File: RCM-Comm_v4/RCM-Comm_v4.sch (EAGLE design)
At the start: 27 parts, among them J1 BLACKFIN_HEADER, J2 2199230-4

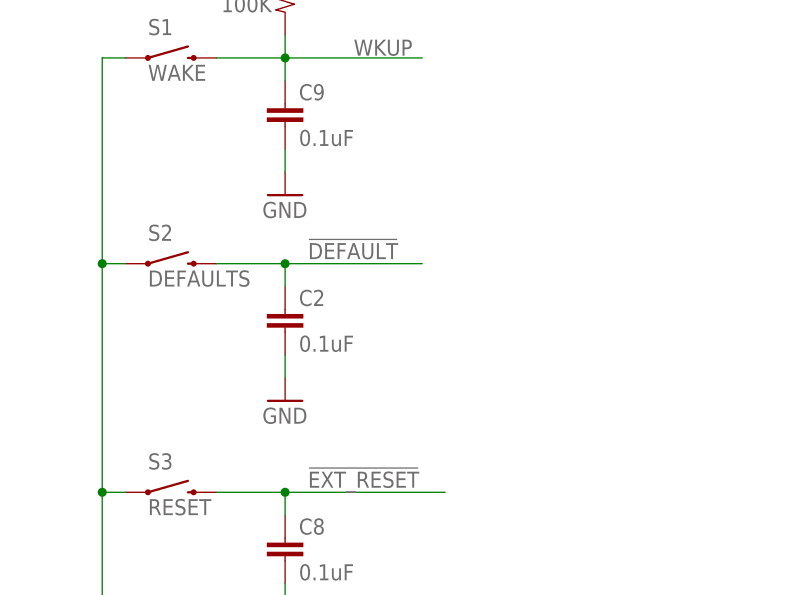
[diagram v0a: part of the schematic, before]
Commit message: Added DEFAULT ENABLE header back in, re-rendered top and bottom for approval.
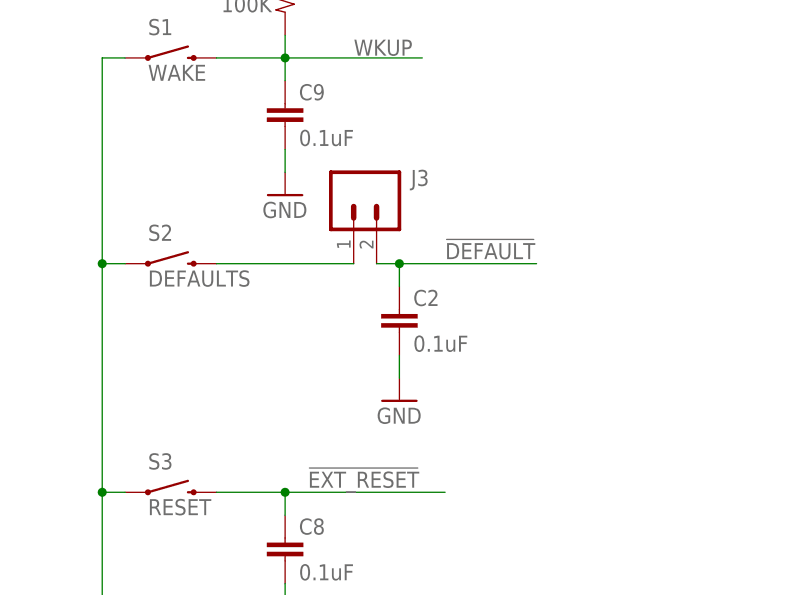
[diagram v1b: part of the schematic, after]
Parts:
- added J3: (no value), SparkFun-Connectors:CONN_02
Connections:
- new net N$1: J3.1, S2.2
- net !DEFAULT!: now also J3.2; no longer S2.2
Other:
- note added: "12/24/2018 v4.0 first release - Swapped radios to xPico 240 with new M.2 connector - removed extra circutry that 240 doesn't support"
- note added: "Connect to allow default button to work"
- note added: "xPico 240 with M.2 connector"
- note removed: "05/30/16 BPS Removed big holes with copper ring, added same dia but normal holes, moved them so they sit better on other boards in the stack."
- moved on the sheet: C2
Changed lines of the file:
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@@
 <layer number="230" name="230bmp" color="7" fill="1" visible="no" active="yes"/>
 <layer number="231" name="231bmp" color="7" fill="1" visible="no" active="yes"/>
+<layer number="232" name="Eagle3D_PG2" color="7" fill="1" visible="yes" active="yes"/>
+<layer number="233" name="Eagle3D_PG3" color="7" fill="1" visible="yes" active="yes"/>
 <layer number="248" name="Housing" color="7" fill="1" visible="yes" active="yes"/>
 <layer number="249" name="Edge" color="7" fill="1" visible="yes" active="yes"/>
@@
 <part name="R10" library="spark_fun" deviceset="RESISTOR" device="0603-RES" value="100K"/>
 <part name="P+10" library="spark_fun" deviceset="VCC" device=""/>
+<part name="J3" library="SparkFun-Connectors" library_urn="urn:adsk.eagle:library:513" deviceset="CONN_02" device="" package3d_urn="urn:adsk.eagle:package:38039/1"/>
 </parts>
 <sheets>
@@
 governing permissions and limitations under the License.</text>
 <text x="5.08" y="177.8" size="5.08" layer="94">RCM-Comm Board v4.0</text>
-<text x="139.7" y="180.34" size="1.27" layer="98">05/30/16 BPS Removed big holes with copper ring, added same dia but normal holes,
-moved them so they sit better on other boards in the stack.</text>
+<text x="114.3" y="167.64" size="1.27" layer="98">12/24/2018 v4.0 first release
+  - Swapped radios to xPico 240 with new M.2 connector
+  - removed extra circutry that 240 doesn't support</text>
+<text x="113.03" y="77.47" size="1.778" layer="98">Connect to allow default button to work</text>
+<text x="193.04" y="58.42" size="1.778" layer="98">xPico 240 with M.2 connector</text>
 </plain>
 <instances>
@@
 <attribute name="VALUE" x="76.2" y="27.94" size="1.778" layer="96"/>
 </instance>
-<instance part="C2" gate="G$1" x="99.06" y="63.5" smashed="yes">
-<attribute name="NAME" x="100.584" y="66.421" size="1.778" layer="95"/>
-<attribute name="VALUE" x="100.584" y="61.341" size="1.778" layer="96"/>
+<instance part="C2" gate="G$1" x="111.76" y="63.5" smashed="yes">
+<attribute name="NAME" x="113.284" y="66.421" size="1.778" layer="95"/>
+<attribute name="VALUE" x="113.284" y="61.341" size="1.778" layer="96"/>
 </instance>
 <instance part="C8" gate="G$1" x="99.06" y="38.1" smashed="yes">
@@
 <attribute name="VALUE" x="100.584" y="84.201" size="1.778" layer="96"/>
 </instance>
-<instance part="GND10" gate="1" x="99.06" y="55.88" smashed="yes">
-<attribute name="VALUE" x="96.52" y="53.34" size="1.778" layer="96"/>
+<instance part="GND10" gate="1" x="111.76" y="55.88" smashed="yes">
+<attribute name="VALUE" x="109.22" y="53.34" size="1.778" layer="96"/>
 </instance>
 <instance part="GND11" gate="1" x="99.06" y="30.48" smashed="yes">
@@
 <instance part="P+10" gate="1" x="7.62" y="35.56" smashed="yes">
 <attribute name="VALUE" x="7.874" y="35.56" size="1.778" layer="96" rot="R270"/>
+</instance>
+<instance part="J3" gate="G$1" x="106.68" y="78.74" smashed="yes" rot="R270">
+<attribute name="VALUE" x="101.854" y="81.28" size="1.778" layer="96" font="vector" rot="R270"/>
+<attribute name="NAME" x="113.03" y="79.756" size="1.778" layer="95" font="vector"/>
 </instance>
 </instances>
@@
 <pinref part="C2" gate="G$1" pin="2"/>
 <pinref part="GND10" gate="1" pin="GND"/>
-<wire x1="99.06" y1="60.96" x2="99.06" y2="58.42" width="0.1524" layer="91"/>
+<wire x1="111.76" y1="60.96" x2="111.76" y2="58.42" width="0.1524" layer="91"/>
 </segment>
 <segment>
@@
 <net name="!DEFAULT!" class="0">
 <segment>
-<pinref part="S2" gate="G$1" pin="2"/>
-<wire x1="91.44" y1="71.12" x2="99.06" y2="71.12" width="0.1524" layer="91"/>
-<label x="101.6" y="71.628" size="1.778" layer="95"/>
+<label x="116.84" y="71.628" size="1.778" layer="95"/>
 <pinref part="C2" gate="G$1" pin="1"/>
-<wire x1="99.06" y1="71.12" x2="114.3" y2="71.12" width="0.1524" layer="91"/>
-<wire x1="99.06" y1="68.58" x2="99.06" y2="71.12" width="0.1524" layer="91"/>
-<junction x="99.06" y="71.12"/>
+<wire x1="111.76" y1="71.12" x2="127" y2="71.12" width="0.1524" layer="91"/>
+<wire x1="111.76" y1="68.58" x2="111.76" y2="71.12" width="0.1524" layer="91"/>
+<pinref part="J3" gate="G$1" pin="2"/>
+<wire x1="109.22" y1="71.12" x2="111.76" y2="71.12" width="0.1524" layer="91"/>
+<junction x="111.76" y="71.12"/>
 </segment>
 <segment>
@@
 <wire x1="20.32" y1="30.48" x2="30.48" y2="30.48" width="0.1524" layer="91"/>
 <label x="22.86" y="30.48" size="1.778" layer="95"/>
+</segment>
+</net>
+<net name="N$1" class="0">
+<segment>
+<pinref part="S2" gate="G$1" pin="2"/>
+<pinref part="J3" gate="G$1" pin="1"/>
+<wire x1="91.44" y1="71.12" x2="106.68" y2="71.12" width="0.1524" layer="91"/>
 </segment>
 </net>
@@
 which will not be processed correctly with this version.
 </note>
+<note version="8.2" severity="warning">
+Since Version 8.2, EAGLE supports online libraries. The ids
+of those online libraries will not be understood (or retained)
+with this version.
+</note>
+<note version="8.3" severity="warning">
+Since Version 8.3, EAGLE supports URNs for individual library
+assets (packages, symbols, and devices). The URNs of those assets
+will not be understood (or retained) with this version.
+</note>
+<note version="8.3" severity="warning">
+Since Version 8.3, EAGLE supports the association of 3D packages
+with devices in libraries, schematics, and board files. Those 3D
+packages will not be understood (or retained) with this version.
+</note>
 </compatibility>

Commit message: Added WLAN Led on configurable pin (CP) #1.
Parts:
- added LED3: GREEN, spark_fun:LED0603
- added R1: 330, spark_fun:RESISTOR0603-RES
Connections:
- removed net N$68: J2.50
- new net N$2: LED3.A, R1.2
- new net WLAN0: J2.50, R1.1
- net GND: now also LED3.C
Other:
- moved on the sheet: LED1, LED2, R3, R5
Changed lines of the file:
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@@
 <part name="P+10" library="spark_fun" deviceset="VCC" device=""/>
 <part name="J3" library="SparkFun-Connectors" library_urn="urn:adsk.eagle:library:513" deviceset="CONN_02" device="" package3d_urn="urn:adsk.eagle:package:38039/1"/>
+<part name="R1" library="spark_fun" deviceset="RESISTOR" device="0603-RES" value="330"/>
+<part name="LED3" library="spark_fun" deviceset="LED" device="0603" value="GREEN"/>
+<part name="GND1" library="supply1" deviceset="GND" device=""/>
 </parts>
 <sheets>
@@
 <attribute name="NAME" x="52.07" y="150.622" size="1.778" layer="95"/>
 </instance>
-<instance part="LED1" gate="G$1" x="15.24" y="76.2" smashed="yes">
-<attribute name="NAME" x="4.826" y="75.184" size="1.778" layer="95"/>
-<attribute name="VALUE" x="3.048" y="72.009" size="1.778" layer="96"/>
-</instance>
-<instance part="LED2" gate="G$1" x="55.88" y="60.96" smashed="yes">
-<attribute name="NAME" x="45.72" y="60.706" size="1.778" layer="95"/>
-<attribute name="VALUE" x="43.688" y="56.769" size="1.778" layer="96"/>
+<instance part="LED1" gate="G$1" x="15.24" y="73.66" smashed="yes">
+<attribute name="NAME" x="4.826" y="72.644" size="1.778" layer="95"/>
+<attribute name="VALUE" x="3.048" y="69.469" size="1.778" layer="96"/>
+</instance>
+<instance part="LED2" gate="G$1" x="66.04" y="60.96" smashed="yes">
+<attribute name="NAME" x="55.88" y="60.706" size="1.778" layer="95"/>
+<attribute name="VALUE" x="53.848" y="56.769" size="1.778" layer="96"/>
 </instance>
 <instance part="GND2" gate="1" x="45.72" y="101.6" smashed="yes">
@@
 <attribute name="VALUE" x="40.64" y="2.54" size="1.778" layer="96"/>
 </instance>
-<instance part="R3" gate="G$1" x="15.24" y="63.5" smashed="yes" rot="R90">
-<attribute name="NAME" x="9.652" y="64.2366" size="1.778" layer="95"/>
-<attribute name="VALUE" x="8.382" y="60.96" size="1.778" layer="96"/>
-</instance>
-<instance part="R5" gate="G$1" x="55.88" y="71.12" smashed="yes" rot="R270">
-<attribute name="NAME" x="50.038" y="71.6026" size="1.778" layer="95"/>
-<attribute name="VALUE" x="48.768" y="68.58" size="1.778" layer="96"/>
+<instance part="R3" gate="G$1" x="15.24" y="60.96" smashed="yes" rot="R90">
+<attribute name="NAME" x="9.652" y="61.6966" size="1.778" layer="95"/>
+<attribute name="VALUE" x="8.382" y="58.42" size="1.778" layer="96"/>
+</instance>
+<instance part="R5" gate="G$1" x="66.04" y="71.12" smashed="yes" rot="R270">
+<attribute name="NAME" x="60.198" y="71.6026" size="1.778" layer="95"/>
+<attribute name="VALUE" x="58.928" y="68.58" size="1.778" layer="96"/>
 </instance>
 <instance part="FRAME1" gate="G$1" x="0" y="0" smashed="yes"/>
@@
 <attribute name="VALUE" x="87.884" y="13.081" size="1.778" layer="96"/>
 </instance>
-<instance part="GND6" gate="1" x="55.88" y="50.8" smashed="yes">
-<attribute name="VALUE" x="53.34" y="48.26" size="1.778" layer="96"/>
+<instance part="GND6" gate="1" x="66.04" y="50.8" smashed="yes">
+<attribute name="VALUE" x="63.5" y="48.26" size="1.778" layer="96"/>
 </instance>
 <instance part="S1" gate="G$1" x="86.36" y="93.98" smashed="yes">
@@
 <attribute name="VALUE" x="101.854" y="81.28" size="1.778" layer="96" font="vector" rot="R270"/>
 <attribute name="NAME" x="113.03" y="79.756" size="1.778" layer="95" font="vector"/>
+</instance>
+<instance part="R1" gate="G$1" x="40.64" y="71.12" smashed="yes" rot="R270">
+<attribute name="NAME" x="34.798" y="71.6026" size="1.778" layer="95"/>
+<attribute name="VALUE" x="33.528" y="68.58" size="1.778" layer="96"/>
+</instance>
+<instance part="LED3" gate="G$1" x="40.64" y="60.96" smashed="yes">
+<attribute name="NAME" x="30.48" y="60.706" size="1.778" layer="95"/>
+<attribute name="VALUE" x="28.448" y="56.769" size="1.778" layer="96"/>
+</instance>
+<instance part="GND1" gate="1" x="40.64" y="50.8" smashed="yes">
+<attribute name="VALUE" x="38.1" y="48.26" size="1.778" layer="96"/>
 </instance>
 </instances>
@@
 </segment>
 <segment>
-<wire x1="15.24" y1="58.42" x2="15.24" y2="53.34" width="0.1524" layer="91"/>
+<wire x1="15.24" y1="55.88" x2="15.24" y2="53.34" width="0.1524" layer="91"/>
 <pinref part="GND4" gate="1" pin="GND"/>
 <pinref part="R3" gate="G$1" pin="1"/>
@@
 <pinref part="LED2" gate="G$1" pin="C"/>
 <pinref part="GND6" gate="1" pin="GND"/>
-<wire x1="55.88" y1="55.88" x2="55.88" y2="53.34" width="0.1524" layer="91"/>
+<wire x1="66.04" y1="55.88" x2="66.04" y2="53.34" width="0.1524" layer="91"/>
 </segment>
 <segment>
@@
 <junction x="233.68" y="66.04"/>
 </segment>
+<segment>
+<pinref part="LED3" gate="G$1" pin="C"/>
+<pinref part="GND1" gate="1" pin="GND"/>
+<wire x1="40.64" y1="55.88" x2="40.64" y2="53.34" width="0.1524" layer="91"/>
+</segment>
 </net>
 <net name="VCC" class="0">
@@
 </segment>
 <segment>
-<wire x1="15.24" y1="83.82" x2="15.24" y2="78.74" width="0.1524" layer="91"/>
+<wire x1="15.24" y1="83.82" x2="15.24" y2="76.2" width="0.1524" layer="91"/>
 <pinref part="P+4" gate="1" pin="VCC"/>
 <pinref part="LED1" gate="G$1" pin="A"/>
@@
 <net name="N$3" class="0">
 <segment>
-<wire x1="15.24" y1="71.12" x2="15.24" y2="68.58" width="0.1524" layer="91"/>
+<wire x1="15.24" y1="68.58" x2="15.24" y2="66.04" width="0.1524" layer="91"/>
 <pinref part="LED1" gate="G$1" pin="C"/>
 <pinref part="R3" gate="G$1" pin="2"/>
@@
 <net name="STATUS_LED" class="0">
 <segment>
-<wire x1="38.1" y1="81.28" x2="55.88" y2="81.28" width="0.1524" layer="91"/>
-<wire x1="55.88" y1="81.28" x2="55.88" y2="76.2" width="0.1524" layer="91"/>
-<label x="38.1" y="81.788" size="1.778" layer="95"/>
+<wire x1="48.26" y1="88.9" x2="66.04" y2="88.9" width="0.1524" layer="91"/>
+<wire x1="66.04" y1="88.9" x2="66.04" y2="76.2" width="0.1524" layer="91"/>
+<label x="48.26" y="89.408" size="1.778" layer="95"/>
 <pinref part="R5" gate="G$1" pin="1"/>
 </segment>
@@
 <pinref part="R5" gate="G$1" pin="2"/>
 <pinref part="LED2" gate="G$1" pin="A"/>
-<wire x1="55.88" y1="66.04" x2="55.88" y2="63.5" width="0.1524" layer="91"/>
+<wire x1="66.04" y1="66.04" x2="66.04" y2="63.5" width="0.1524" layer="91"/>
 </segment>
 </net>
@@
 </segment>
 </net>
-<net name="N$68" class="0">
-<segment>
-<pinref part="J2" gate="G$1" pin="50"/>
-<wire x1="193.04" y1="119.38" x2="187.96" y2="119.38" width="0.1524" layer="91"/>
-</segment>
-</net>
 <net name="N$69" class="0">
 <segment>
@@
 </segment>
 </net>
+<net name="N$2" class="0">
+<segment>
+<pinref part="R1" gate="G$1" pin="2"/>
+<pinref part="LED3" gate="G$1" pin="A"/>
+<wire x1="40.64" y1="66.04" x2="40.64" y2="63.5" width="0.1524" layer="91"/>
+</segment>
+</net>
+<net name="WLAN0" class="0">
+<segment>
+<pinref part="R1" gate="G$1" pin="1"/>
+<wire x1="40.64" y1="76.2" x2="40.64" y2="81.28" width="0.1524" layer="91"/>
+<wire x1="40.64" y1="81.28" x2="25.4" y2="81.28" width="0.1524" layer="91"/>
+<label x="25.4" y="81.28" size="1.778" layer="95"/>
+</segment>
+<segment>
+<pinref part="J2" gate="G$1" pin="50"/>
+<wire x1="193.04" y1="119.38" x2="172.72" y2="119.38" width="0.1524" layer="91"/>
+<label x="172.72" y="119.38" size="1.778" layer="95"/>
+</segment>
+</net>

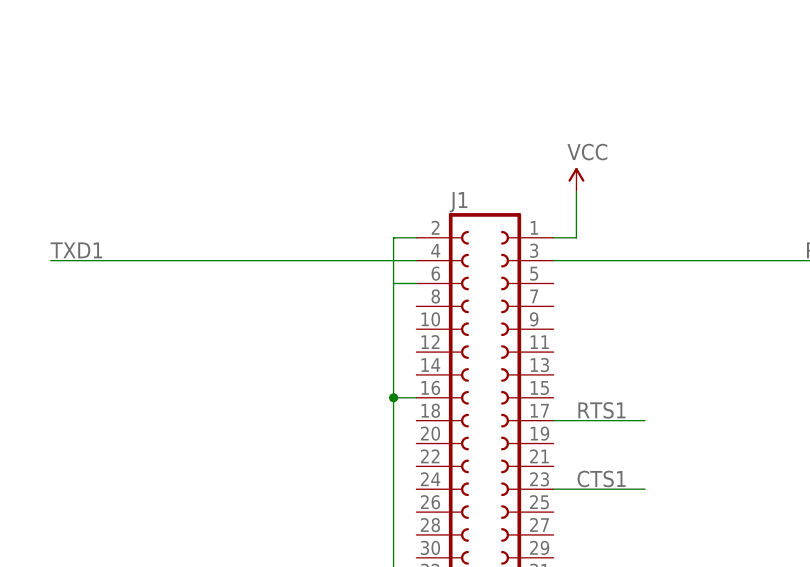
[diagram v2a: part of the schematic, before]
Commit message: Updated final BOM. Final 'd' version of gerbers, which got sent to JLCPCB.
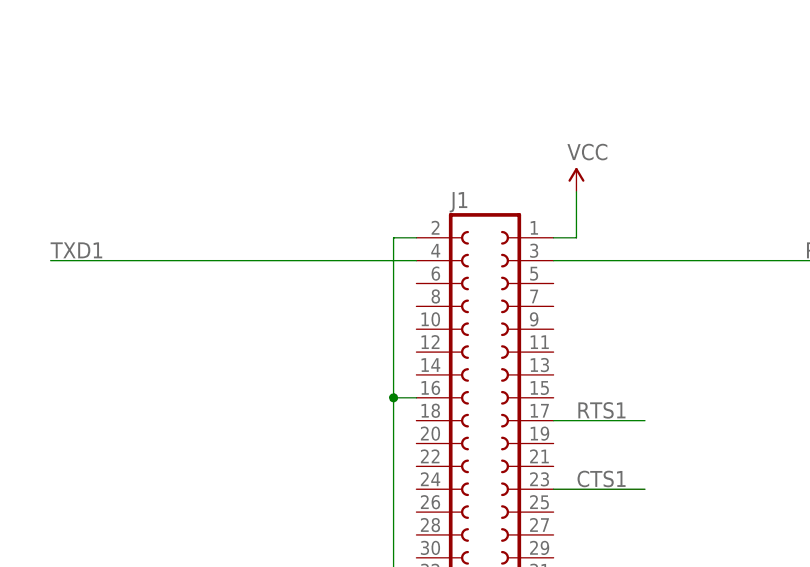
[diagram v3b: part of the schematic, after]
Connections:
- removed net N$24: J1.RX1
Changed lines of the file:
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@@
-</segment>
-</net>
-<net name="N$24" class="0">
-<segment>
-<wire x1="45.72" y1="142.24" x2="48.26" y2="142.24" width="0.1524" layer="91"/>
-<pinref part="J1" gate="G$1" pin="RX1"/>
 </segment>
 </net>
